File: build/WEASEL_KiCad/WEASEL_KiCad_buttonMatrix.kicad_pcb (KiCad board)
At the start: 2 copper layers, 125.5 x 75 mm, 42 parts, among them J1 Conn_02x10_Odd_Even, SW1 SQ_TOGGLESTEP1, SW2 SEQ_TRIGGERSELECT, SW3 SQ_TOGGLESTEP2, SW31 EG_TRIGGERSELECT, SW32 EG_MODESELECT, SW33 PLSR_TRIGGERSELECT, SW34 PLSR_MODE, SW35 MODOSC_MIDITOGGLE, SW36 MODOSC_PITCHTRANGE, SW37 COMPLEXOSC_MIDITOGGLE, SW38 COMPLEXOSC_POLARITY, SW39 COMPLEXOSC_WAVETOGGLE, SW4 SQ_TOGGLESTEP3, SW40 LPG_GATE1MODE, SW41 LPG_GATE2MODE, SW42 RNDMVOLTAGE_TRIGGERSELECT, SW43 CLOCK_SYNCTOGGLE, SW5 SQ_TOGGLESTEP4, SW6 SEQ_STAGES, SW7 SQ_TOGGLESTEP5

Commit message: Button Matrix Prototype Update
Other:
- board text added: "CLOCK SYNC TOGGLE FREE / SYNC"
- board text added: "COMP OSC MIDI TOGGLE ON / OFF"
- board text added: "COMP OSC POLARITY + / -"
- board text added: "COMP OSC WAVEFORM SAW / SQU / TRI"
- board text added: "EG MODE TRANS / SUST / SELF-OSC"
- board text added: "EG TRIGGER MODE MIDI / PLSR / SQ"
- board text added: "LPG CH1 MODE COMBI / VCA / LP"
- board text added: "MOD OSC MIDI TOGGLE ON / OFF"
- board text added: "MOD OSC PITCH RANGE HIGH / LOW"
- board text added: "PLSR MODE FREE / CLK"
- board text added: "PLSR TRIGGER MODE MIDI / PLSR / SQ"
- board text added: "RNDM VOLT TRIGGER MODE MIDI / PLSR / SEQUENCER"
- board text added: "SQ NUM. STEPS 5 / 4 / 3"
- board text added: "SQ TRIGGER MODE MIDI / PLSR / CLK"
- board text added: "STEP 1"
- board text added: "STEP 2"
- board text added: "STEP 3"
- board text added: "STEP 4"
- board text added: "STEP 5"

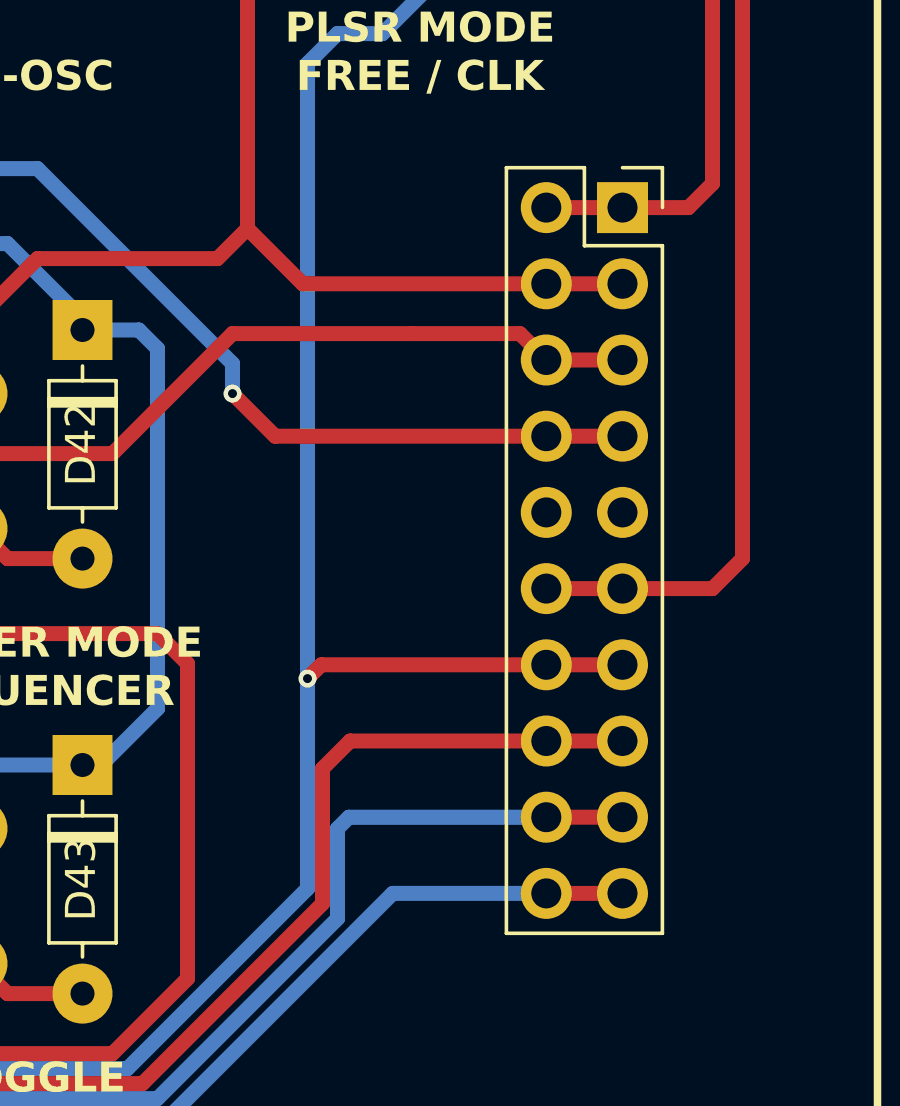
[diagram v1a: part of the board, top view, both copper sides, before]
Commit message: PCB Button Matrix Update
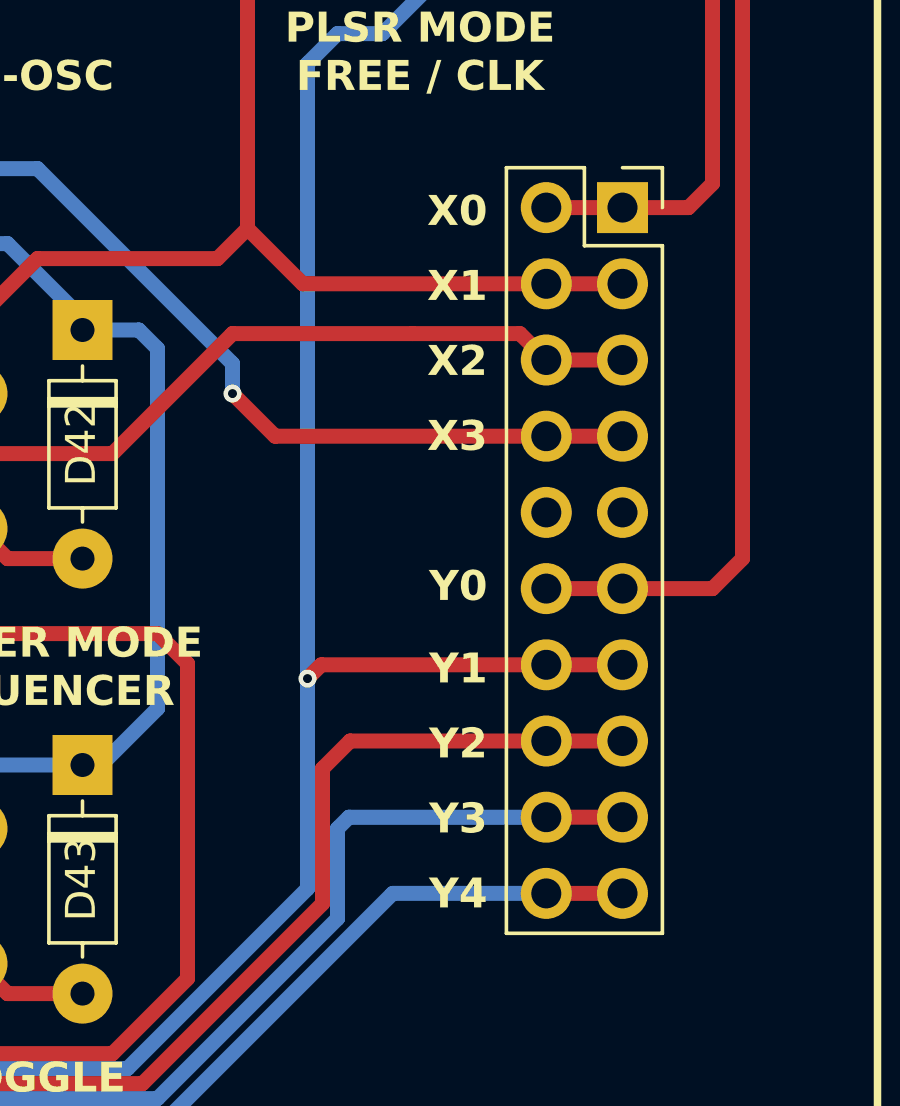
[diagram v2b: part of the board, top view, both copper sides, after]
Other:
- board text added: "X0"
- board text added: "X1"
- board text added: "X2"
- board text added: "X3"
- board text added: "Y0"
- board text added: "Y1"
- board text added: "Y2"
- board text added: "Y3"
- board text added: "Y4"
